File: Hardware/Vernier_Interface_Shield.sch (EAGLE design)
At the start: 41 parts, among them U1 74HC4052SO, U2 LMV358

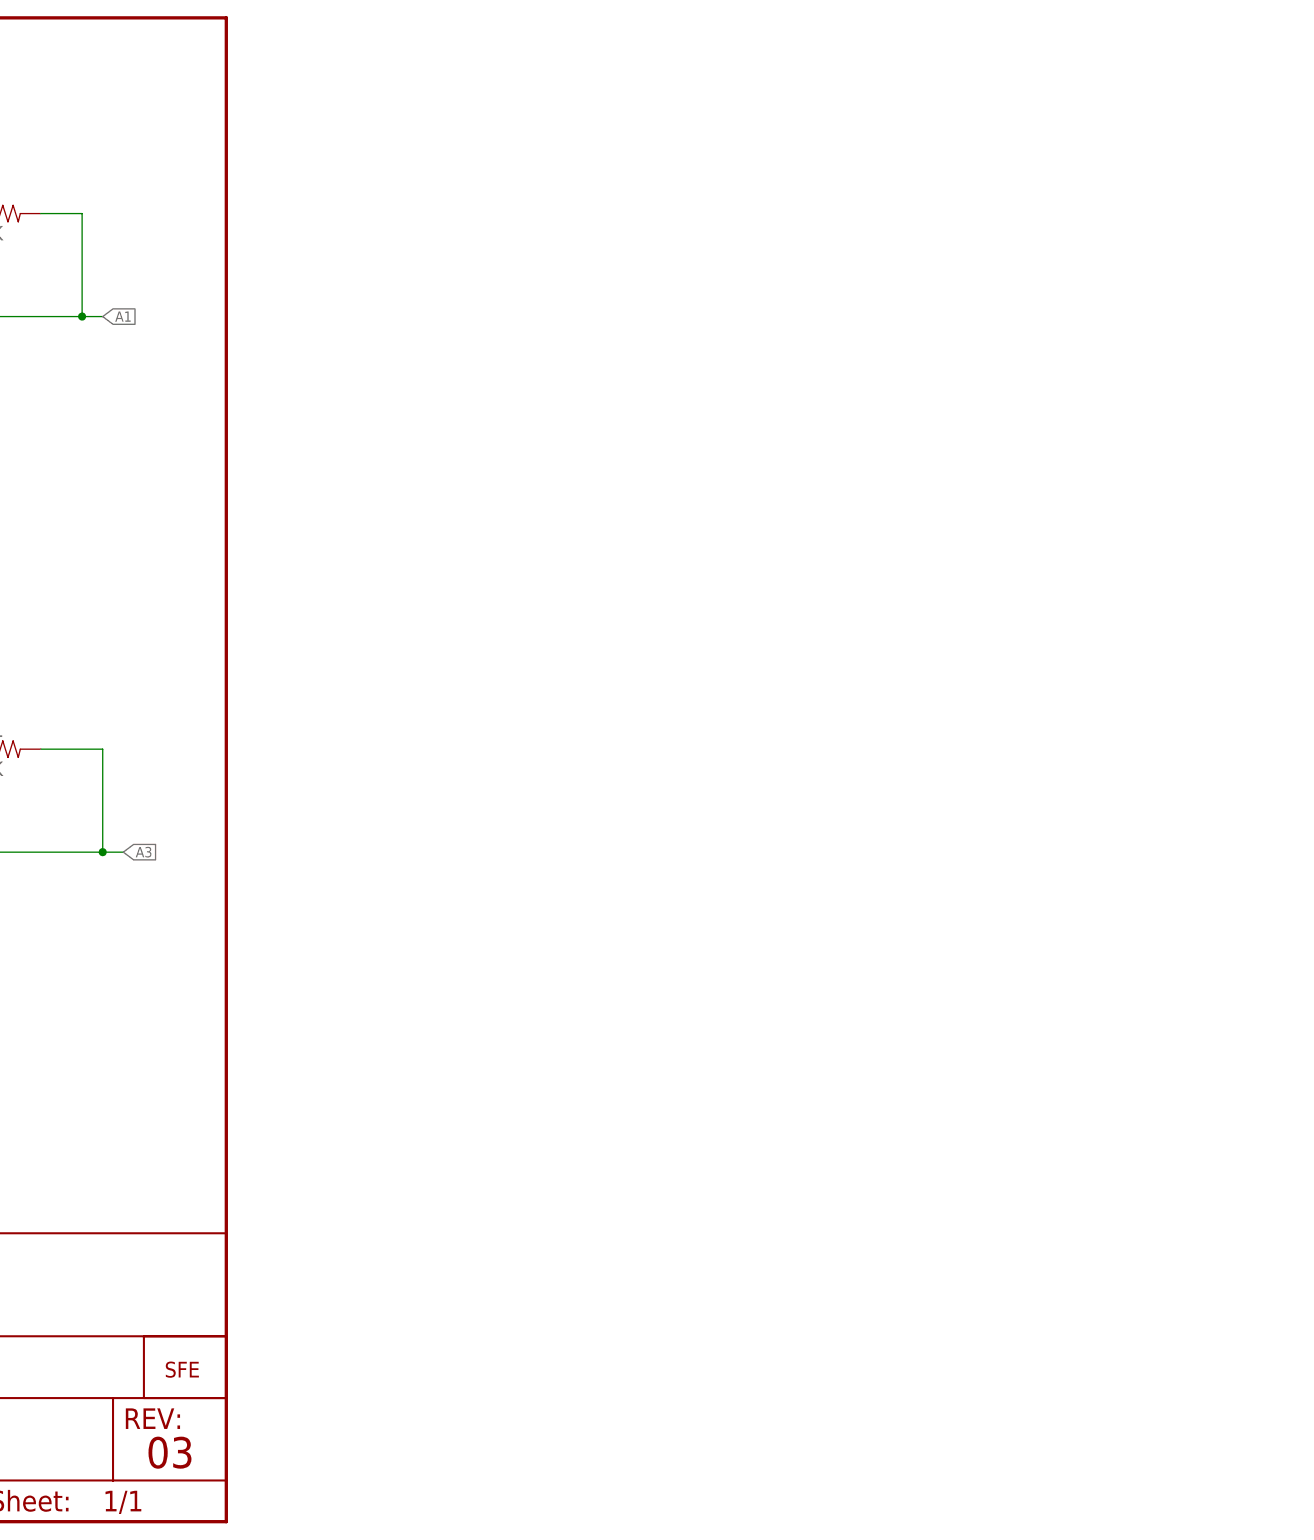
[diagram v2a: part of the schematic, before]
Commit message: Switched Digital 1 and Digital 2 on the Board
Fixed the Digital 1 and Digital 2. V03 had the two connectors flipped.
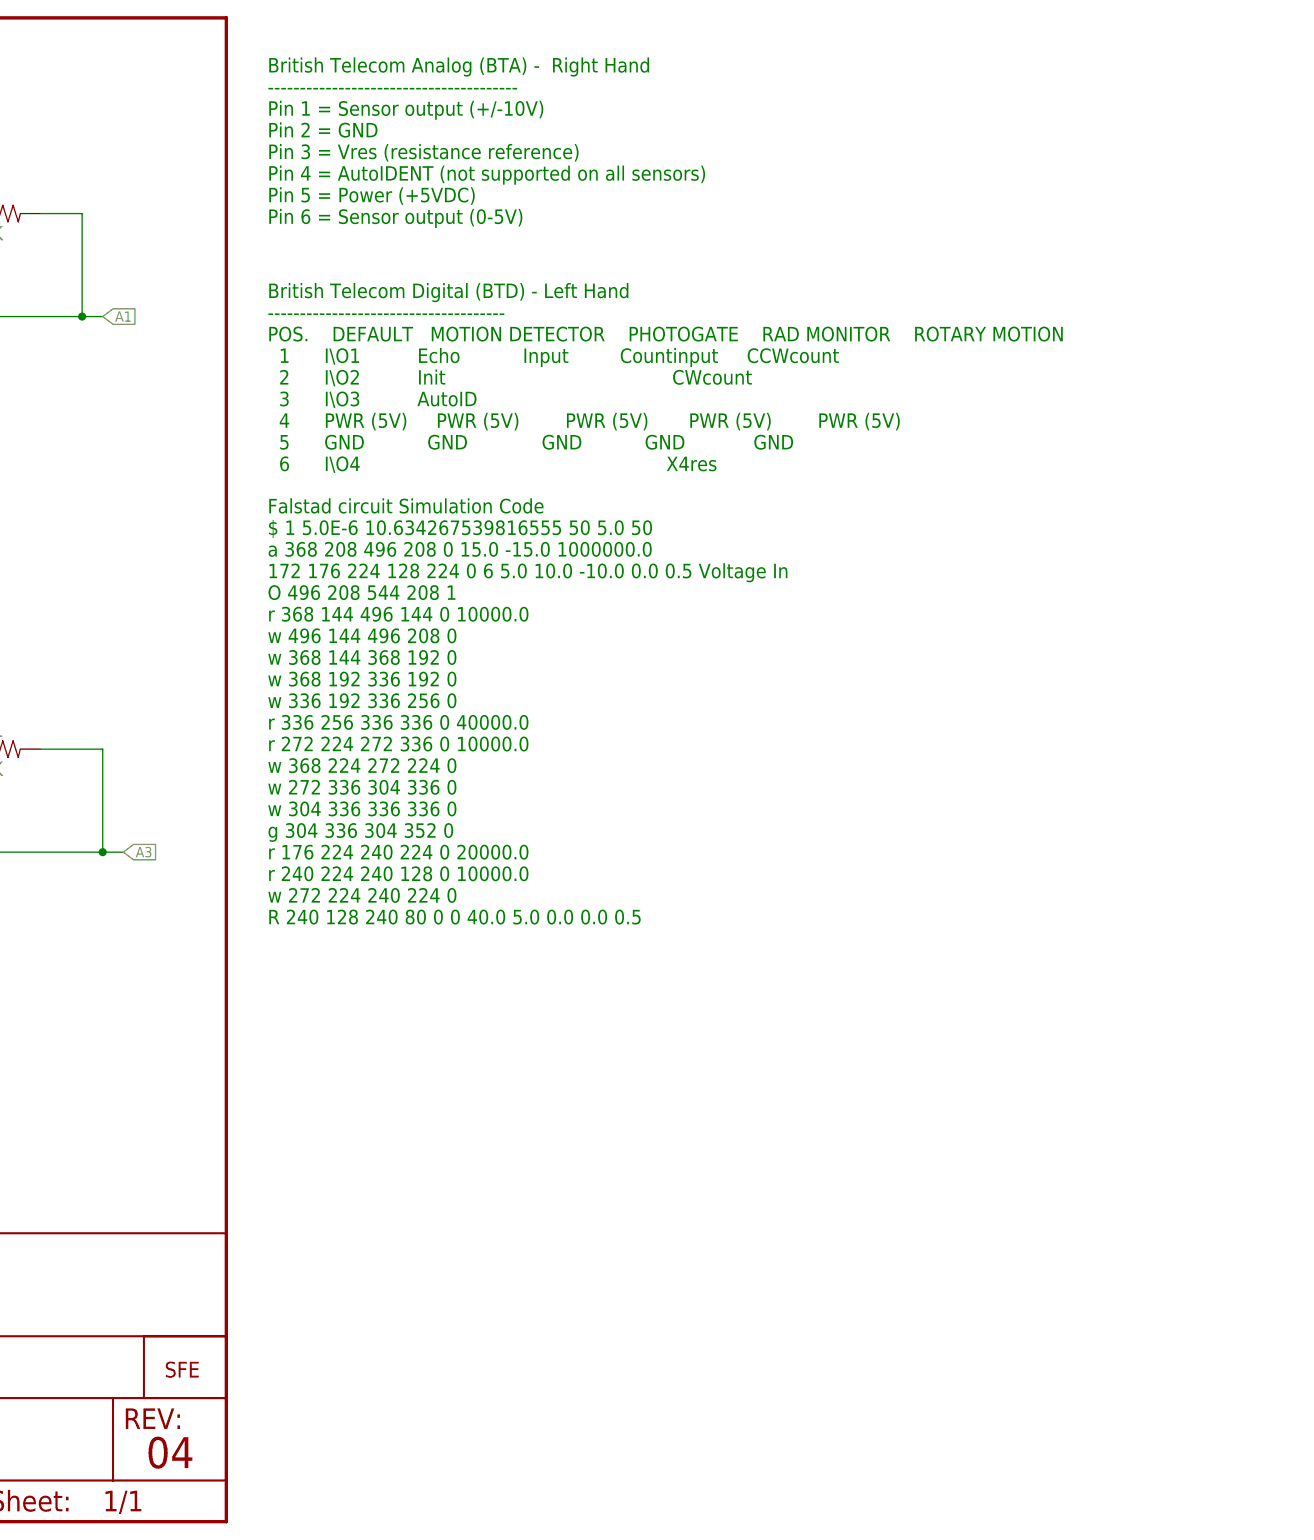
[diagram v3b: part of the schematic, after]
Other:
- note added: "04"
- note added: "British Telecom Analog (BTA) - Right Hand --------------------------------------- Pin 1 = Sensor output (+/-10V) Pin 2 = GND Pin 3 = Vres (resistance reference) Pin 4 = AutoIDENT (not supported on all sensors) Pin 5 = Power (+5VDC) Pin 6 = Sensor output (0-5V)"
- note added: "British Telecom Digital (BTD) - Left Hand ------------------------------------- POS. DEFAULT MOTION DETECTOR PHOTOGATE RAD MONITOR ROTARY MOTION 1 I\\O1 Echo Input Countinput CCWcount 2 I\\O2 Init CWcount 3 I\\O3 AutoID 4 PWR (5V) PWR (5V) PWR (5V) PWR (5V) PWR (5V) 5 GND GND GND GND GND 6 I\\O4 X4res"
- note added: "Falstad circuit Simulation Code $ 1 5.0E-6 10.634267539816555 50 5.0 50 a 368 208 496 208 0 15.0 -15.0 1000000.0 172 176 224 128 224 0 6 5.0 10.0 -10.0 0.0 0.5 Voltage In O 496 208 544 208 1 r 368 144 496 144 0 10000.0 w 496 144 496 208 0 w 368 144 368 192 0 w 368 192 336 192 0 w 336 192 336 256 0 r 336 256 336 336 0 40000.0 r 272 224 272 336 0 10000.0 w 368 224 272 224 0 w 272 336 304 336 0 w 30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"
- note removed: "03"
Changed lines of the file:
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@@
 <text x="5.08" y="17.78" size="2.54" layer="91" rot="R90">DIG 2</text>
 <text x="170.942" y="7.62" size="3.81" layer="94">M. Hord</text>
-<text x="239.014" y="6.604" size="3.81" layer="94">03</text>
+<text x="239.014" y="6.604" size="3.81" layer="94">04</text>
+<text x="254" y="160.02" size="1.778" layer="91">British Telecom Analog (BTA) -  Right Hand
+---------------------------------------
+Pin 1 = Sensor output (+/-10V)
+Pin 2 = GND
+Pin 3 = Vres (resistance reference)
+Pin 4 = AutoIDENT (not supported on all sensors)
+Pin 5 = Power (+5VDC)
+Pin 6 = Sensor output (0-5V)</text>
+<text x="254" y="154.94" size="1.778" layer="91"></text>
+<text x="254" y="129.54" size="1.778" layer="91">British Telecom Digital (BTD) - Left Hand
+-------------------------------------
+POS.    DEFAULT   MOTION DETECTOR    PHOTOGATE    RAD MONITOR    ROTARY MOTION
+  1      I\\O1          Echo           Input         Countinput     CCWcount
+  2      I\\O2          Init                                        CWcount
+  3      I\\O3          AutoID
+  4      PWR (5V)     PWR (5V)        PWR (5V)       PWR (5V)        PWR (5V)
+  5      GND           GND             GND           GND            GND
+  6      I\\O4                                                      X4res</text>
+<text x="254" y="73.66" size="1.778" layer="91">Falstad circuit Simulation Code
+$ 1 5.0E-6 10.634267539816555 50 5.0 50
+a 368 208 496 208 0 15.0 -15.0 1000000.0
+172 176 224 128 224 0 6 5.0 10.0 -10.0 0.0 0.5 Voltage In
+O 496 208 544 208 1
+r 368 144 496 144 0 10000.0
+w 496 144 496 208 0
+w 368 144 368 192 0
+w 368 192 336 192 0
+w 336 192 336 256 0
+r 336 256 336 336 0 40000.0
+r 272 224 272 336 0 10000.0
+w 368 224 272 224 0
+w 272 336 304 336 0
+w 304 336 336 336 0
+g 304 336 304 352 0
+r 176 224 240 224 0 20000.0
+r 240 224 240 128 0 10000.0
+w 272 224 240 224 0
+R 240 128 240 80 0 0 40.0 5.0 0.0 0.0 0.5</text>
 </plain>
 <instances>
@@
 </schematic>
 </drawing>
+<compatibility>
+<note version="6.3" minversion="6.2.2" severity="warning">
+Since Version 6.2.2 text objects can contain more than one line,
+which will not be processed correctly with this version.
+</note>
+</compatibility>
 </eagle>

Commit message: Release version
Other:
- note added: "10"
- note removed: "04"
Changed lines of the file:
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@@
 <?xml version="1.0" encoding="utf-8"?>
 <!DOCTYPE eagle SYSTEM "eagle.dtd">
-<eagle version="6.5.0">
+<eagle version="6.4">
 <drawing>
 <settings>
@@
 <text x="5.08" y="17.78" size="2.54" layer="91" rot="R90">DIG 2</text>
 <text x="170.942" y="7.62" size="3.81" layer="94">M. Hord</text>
-<text x="239.014" y="6.604" size="3.81" layer="94">04</text>
+<text x="239.014" y="6.604" size="3.81" layer="94">10</text>
 <text x="254" y="160.02" size="1.778" layer="91">British Telecom Analog (BTA) -  Right Hand
 ---------------------------------------

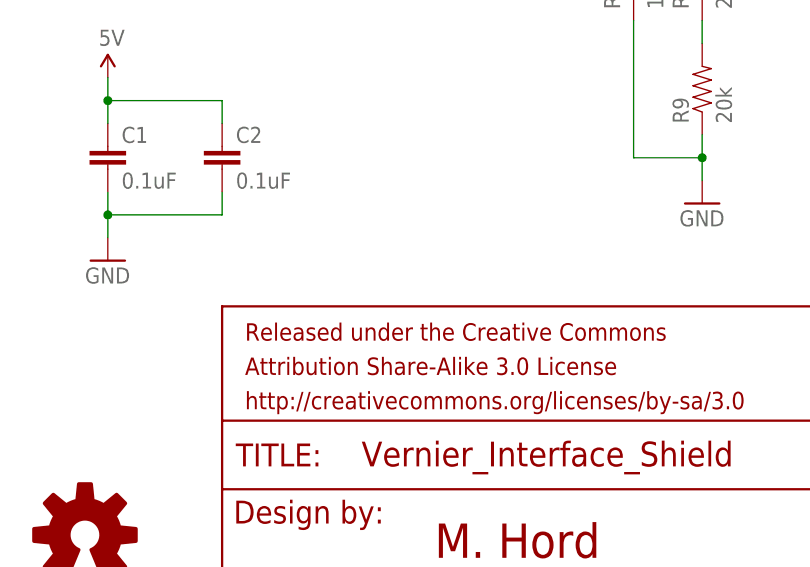
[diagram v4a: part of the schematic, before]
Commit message: Added micro Fiducial to board
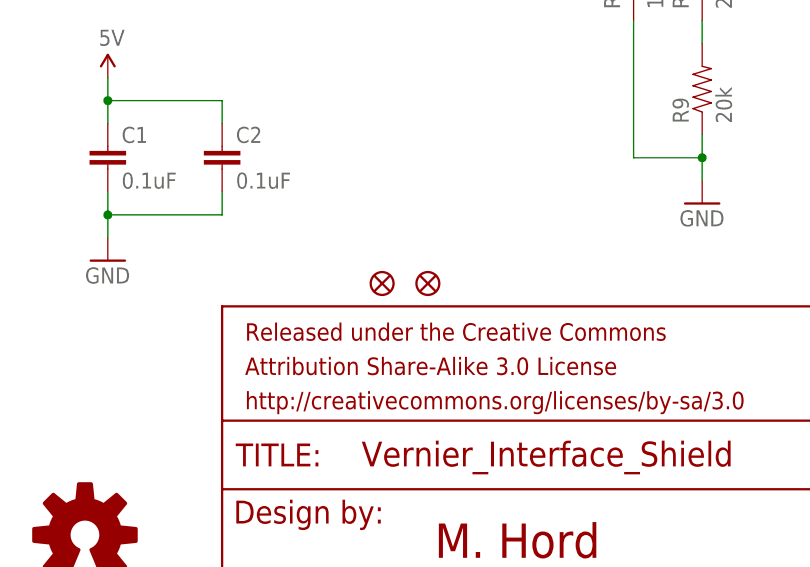
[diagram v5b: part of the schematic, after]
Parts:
- added FID1, FID2: FIDUCIALUFIDUCIAL, SparkFun-Aesthetics:FIDUCIALUFIDUCIAL
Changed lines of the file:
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@@
 <?xml version="1.0" encoding="utf-8"?>
 <!DOCTYPE eagle SYSTEM "eagle.dtd">
-<eagle version="6.4">
+<eagle version="6.5.0">
 <drawing>
 <settings>
@@
 <part name="SUPPLY8" library="SparkFun-Aesthetics" deviceset="5V" device=""/>
 <part name="GND9" library="SparkFun-Aesthetics" deviceset="GND" device=""/>
+<part name="FID1" library="SparkFun-Aesthetics" deviceset="FIDUCIAL" device="UFIDUCIAL"/>
+<part name="FID2" library="SparkFun-Aesthetics" deviceset="FIDUCIAL" device="UFIDUCIAL"/>
 </parts>
 <sheets>
@@
 <instance part="SUPPLY8" gate="G$1" x="99.06" y="172.72"/>
 <instance part="GND9" gate="1" x="99.06" y="134.62"/>
+<instance part="FID1" gate="G$1" x="165.1" y="38.1"/>
+<instance part="FID2" gate="G$1" x="170.18" y="38.1"/>
 </instances>
 <busses>

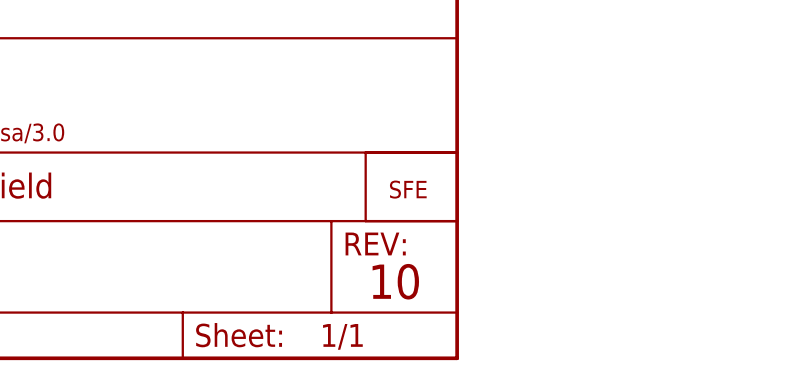
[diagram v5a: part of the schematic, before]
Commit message: Put on grid, rm weird stop on back, to v11
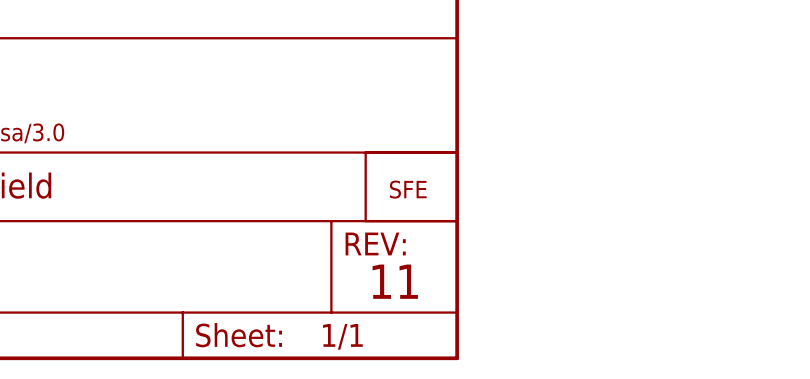
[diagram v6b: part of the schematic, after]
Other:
- note added: "11"
- note removed: "10"
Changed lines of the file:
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@@
 <?xml version="1.0" encoding="utf-8"?>
 <!DOCTYPE eagle SYSTEM "eagle.dtd">
-<eagle version="6.5.0">
+<eagle version="6.4">
 <drawing>
 <settings>
@@
 <text x="5.08" y="17.78" size="2.54" layer="91" rot="R90">DIG 2</text>
 <text x="170.942" y="7.62" size="3.81" layer="94">M. Hord</text>
-<text x="239.014" y="6.604" size="3.81" layer="94">10</text>
+<text x="239.014" y="6.604" size="3.81" layer="94">11</text>
 <text x="254" y="160.02" size="1.778" layer="91">British Telecom Analog (BTA) -  Right Hand
 ---------------------------------------

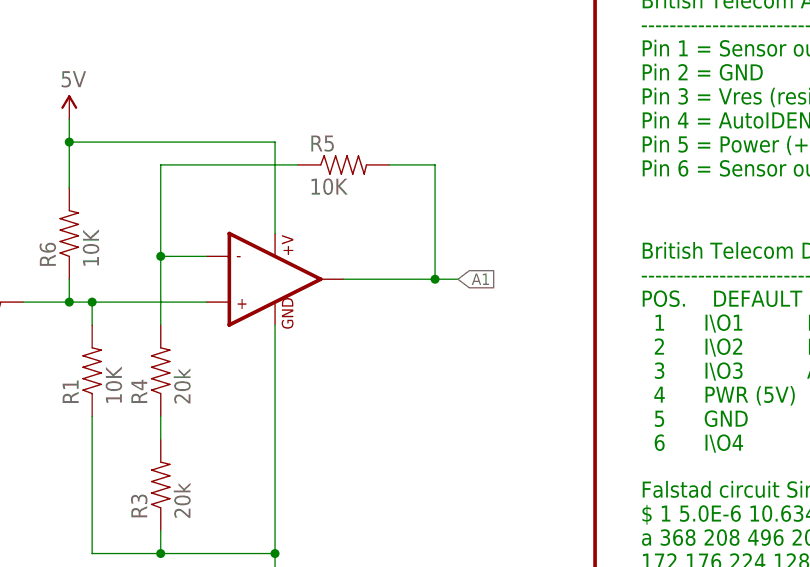
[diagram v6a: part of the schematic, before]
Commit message: Updated connector FPs. Tented some vias. Removed extra silk.
The A5 to A0 labels were of different size and didn't see to go
anywhere. Removed them.
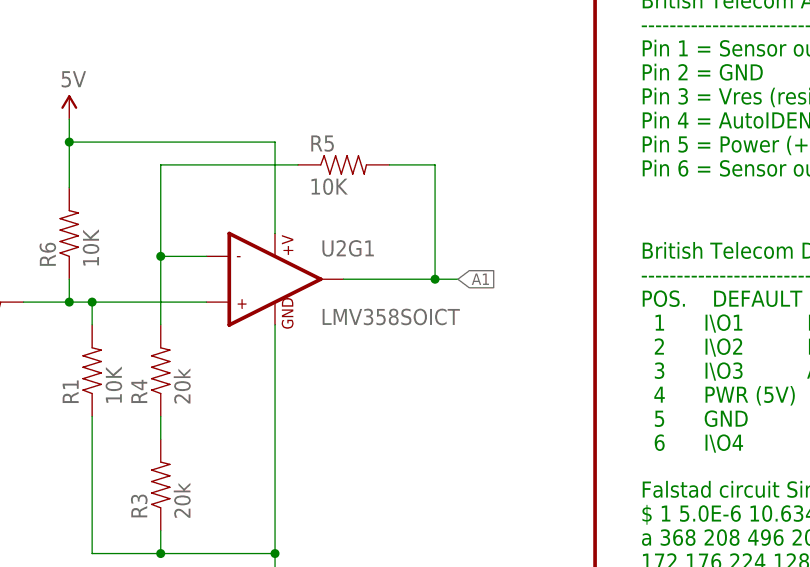
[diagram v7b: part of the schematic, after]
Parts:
- U2: value LMV358 -> LMV358SOICT; device SparkFun-AnalogIC:LMV358 -> SparkFun-AnalogIC:LMV358SOICT
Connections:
- net 5V: now also U2G1.+V; no longer U2G$1.+V
- net A1: now also U2G1.OUT1; no longer U2G$1.OUT1
- net A3: now also U2G2.OUT2; no longer U2G$2.OUT2
- net GND: now also U2G1.GND; no longer U2G$1.GND
- net N$1: now also U2G1.+IN1; no longer U2G$1.+IN1
- net N$3: now also U2G1.-IN1; no longer U2G$1.-IN1
- net N$6: now also U2G2.+IN2; no longer U2G$2.+IN2
- net N$8: now also U2G2.-IN2; no longer U2G$2.-IN2
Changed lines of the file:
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@@
 <?xml version="1.0" encoding="utf-8"?>
 <!DOCTYPE eagle SYSTEM "eagle.dtd">
-<eagle version="6.4">
+<eagle version="6.5.0">
 <drawing>
 <settings>
@@
 <part name="SUPPLY1" library="SparkFun-Aesthetics" deviceset="5V" device=""/>
 <part name="GND1" library="SparkFun-Aesthetics" deviceset="GND" device=""/>
-<part name="U2" library="SparkFun-AnalogIC" deviceset="LMV358" device=""/>
+<part name="U2" library="SparkFun-AnalogIC" deviceset="LMV358" device="SOICT"/>
 <part name="R7" library="SparkFun-Resistors" deviceset="10KOHM1/10W1%(0603)" device="0603" value="10K"/>
 <part name="R8" library="SparkFun-Resistors" deviceset="20KOHM1/10W1%(0603)" device="" value="20k"/>
@@
 <instance part="SUPPLY1" gate="G$1" x="190.5" y="166.37"/>
 <instance part="GND1" gate="1" x="213.36" y="113.03"/>
-<instance part="U2" gate="G$1" x="213.36" y="148.59"/>
-<instance part="U2" gate="G$2" x="213.36" y="82.55"/>
+<instance part="U2" gate="G1" x="213.36" y="148.59"/>
+<instance part="U2" gate="G2" x="213.36" y="82.55"/>
 <instance part="R7" gate="G$1" x="193.04" y="72.39" rot="R90"/>
 <instance part="R8" gate="G$1" x="180.34" y="80.01"/>
@@
 <wire x1="193.04" y1="118.11" x2="200.66" y2="118.11" width="0.1524" layer="91"/>
 <junction x="200.66" y="118.11"/>
-<pinref part="U2" gate="G$1" pin="GND"/>
+<pinref part="U2" gate="G1" pin="GND"/>
 </segment>
 <segment>
@@
 <junction x="190.5" y="163.83"/>
 <wire x1="213.36" y1="163.83" x2="213.36" y2="153.67" width="0.1524" layer="91"/>
-<pinref part="U2" gate="G$1" pin="+V"/>
+<pinref part="U2" gate="G1" pin="+V"/>
 </segment>
 <segment>
@@
 <wire x1="193.04" y1="146.05" x2="205.74" y2="146.05" width="0.1524" layer="91"/>
 <junction x="193.04" y="146.05"/>
-<pinref part="U2" gate="G$1" pin="+IN1"/>
+<pinref part="U2" gate="G1" pin="+IN1"/>
 </segment>
 </net>
@@
 <pinref part="R5" gate="G$1" pin="1"/>
 <wire x1="200.66" y1="161.29" x2="215.9" y2="161.29" width="0.1524" layer="91"/>
-<pinref part="U2" gate="G$1" pin="-IN1"/>
+<pinref part="U2" gate="G1" pin="-IN1"/>
 </segment>
 </net>
@@
 <wire x1="193.04" y1="80.01" x2="205.74" y2="80.01" width="0.1524" layer="91"/>
 <junction x="193.04" y="80.01"/>
-<pinref part="U2" gate="G$2" pin="+IN2"/>
+<pinref part="U2" gate="G2" pin="+IN2"/>
 </segment>
 </net>
@@
 <pinref part="R11" gate="G$1" pin="1"/>
 <wire x1="200.66" y1="95.25" x2="215.9" y2="95.25" width="0.1524" layer="91"/>
-<pinref part="U2" gate="G$2" pin="-IN2"/>
+<pinref part="U2" gate="G2" pin="-IN2"/>
 </segment>
 </net>
@@
 <wire x1="231.14" y1="161.29" x2="231.14" y2="148.59" width="0.1524" layer="91"/>
 <wire x1="231.14" y1="148.59" x2="220.98" y2="148.59" width="0.1524" layer="91"/>
-<pinref part="U2" gate="G$1" pin="OUT1"/>
+<pinref part="U2" gate="G1" pin="OUT1"/>
 <wire x1="231.14" y1="148.59" x2="233.68" y2="148.59" width="0.1524" layer="91"/>
 <junction x="231.14" y="148.59"/>
@@
 <wire x1="233.68" y1="95.25" x2="233.68" y2="82.55" width="0.1524" layer="91"/>
 <wire x1="233.68" y1="82.55" x2="220.98" y2="82.55" width="0.1524" layer="91"/>
-<pinref part="U2" gate="G$2" pin="OUT2"/>
+<pinref part="U2" gate="G2" pin="OUT2"/>
 <wire x1="233.68" y1="82.55" x2="236.22" y2="82.55" width="0.1524" layer="91"/>
 <junction x="233.68" y="82.55"/>
